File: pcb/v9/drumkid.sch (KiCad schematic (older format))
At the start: 57 parts, among them J1 DIN-5_180degree, J2 DIN-5_180degree, J3 Conn_01x15, J4 Conn_01x15, J9 AudioJack3_Ground_Switch, SW1 SW_Push, SW2 SW_Push, SW3 SW_Push, SW4 SW_Push, SW5 SW_Push, SW6 SW_Push, SW7 SW_SPDT, SW8 SW_SPDT, U1 6N138

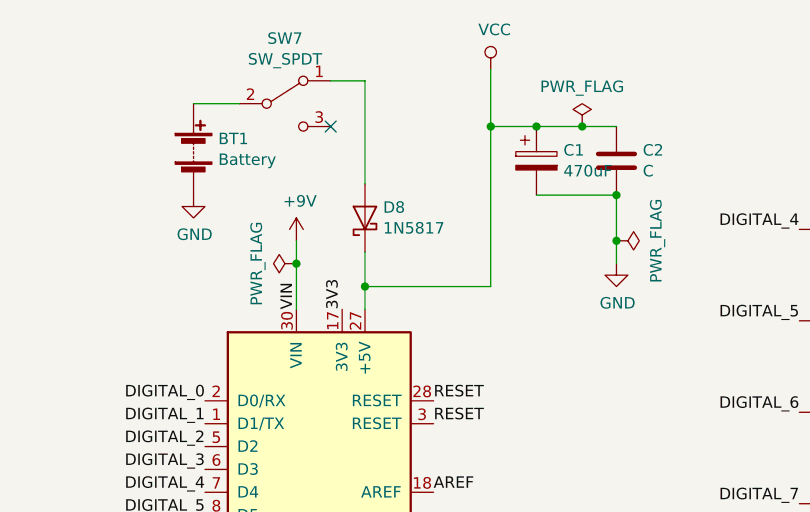
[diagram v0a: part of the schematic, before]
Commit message: added footprints for v9
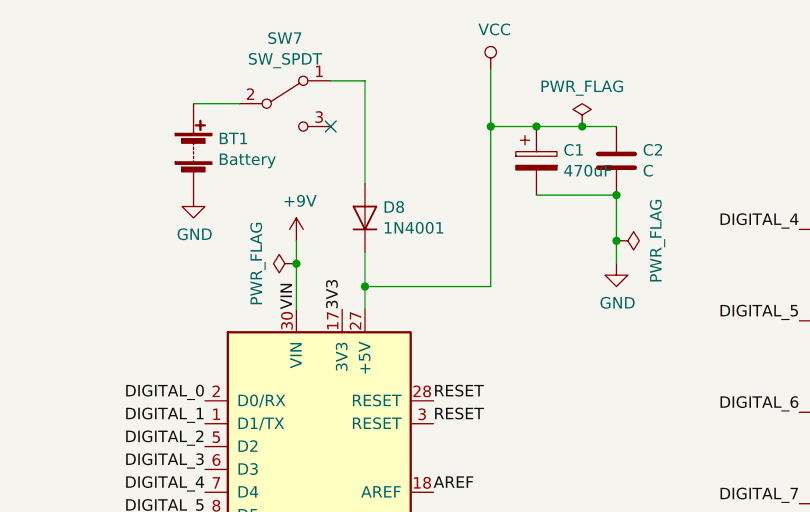
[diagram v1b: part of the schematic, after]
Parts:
- removed D8: 1N5817, symbol Diode:1N5817
- added D8: 1N4001, Diode_SMD:D_SOD-123, symbol Diode:1N4001
- BT1: footprint Connector_Wire:SolderWirePad_1x02_P5.08mm_Drill1.5mm -> Connector_Wire:SolderWire-0.5sqmm_1x02_P4.8mm_D0.9mm_OD2.3mm
- D7: footprint (none) -> Diode_SMD:D_SOD-323
- R1, R10, R11, R12, R13, R2, R3, R4, R5, R6, R7, R8, R9: footprint (none) -> Resistor_SMD:R_1206_3216Metric
- U1: footprint (none) -> Package_DIP:PowerIntegrations_SMD-8
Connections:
- net VCC: now also D8.1 (K)
- net at SW7.1 (A): now also D8.2 (A)
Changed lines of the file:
@@
 Title "DrumKid"
 Date ""
-Rev "v8"
+Rev "v9"
 Comp "by Matt Bradshaw"
 Comment1 ""
@@
 F 0 "R2" V 5243 2050 50  0000 C CNN
 F 1 "680" V 5334 2050 50  0000 C CNN
-F 2 "" V 5380 2050 50  0001 C CNN
+F 2 "Resistor_SMD:R_1206_3216Metric" V 5380 2050 50  0001 C CNN
 F 3 "~" H 5450 2050 50  0001 C CNN
 	1    5450 2050
@@
 F 0 "BT1" H 1558 1346 50  0000 L CNN
 F 1 "Battery" H 1558 1255 50  0000 L CNN
-F 2 "Connector_Wire:SolderWirePad_1x02_P5.08mm_Drill1.5mm" V 1450 1360 50  0001 C CNN
+F 2 "Connector_Wire:SolderWire-0.5sqmm_1x02_P4.8mm_D0.9mm_OD2.3mm" V 1450 1360 50  0001 C CNN
 F 3 "~" V 1450 1360 50  0001 C CNN
 	1    1450 1300
@@
 F 0 "R3" V 5243 2450 50  0000 C CNN
 F 1 "680" V 5334 2450 50  0000 C CNN
-F 2 "" V 5380 2450 50  0001 C CNN
+F 2 "Resistor_SMD:R_1206_3216Metric" V 5380 2450 50  0001 C CNN
 F 3 "~" H 5450 2450 50  0001 C CNN
 	1    5450 2450
@@
 F 0 "R4" V 5243 2850 50  0000 C CNN
 F 1 "680" V 5334 2850 50  0000 C CNN
-F 2 "" V 5380 2850 50  0001 C CNN
+F 2 "Resistor_SMD:R_1206_3216Metric" V 5380 2850 50  0001 C CNN
 F 3 "~" H 5450 2850 50  0001 C CNN
 	1    5450 2850
@@
 F 0 "R5" V 5243 3250 50  0000 C CNN
 F 1 "680" V 5334 3250 50  0000 C CNN
-F 2 "" V 5380 3250 50  0001 C CNN
+F 2 "Resistor_SMD:R_1206_3216Metric" V 5380 3250 50  0001 C CNN
 F 3 "~" H 5450 3250 50  0001 C CNN
 	1    5450 3250
@@
 F 0 "R6" V 5243 3650 50  0000 C CNN
 F 1 "680" V 5334 3650 50  0000 C CNN
-F 2 "" V 5380 3650 50  0001 C CNN
+F 2 "Resistor_SMD:R_1206_3216Metric" V 5380 3650 50  0001 C CNN
 F 3 "~" H 5450 3650 50  0001 C CNN
 	1    5450 3650
@@
 Text Label 1500 3700 2    50   ~ 0
 DIGITAL_13
-$Comp
-L Diode:1N5817 D8
-U 1 1 5E76DFE8
-P 2200 1600
-F 0 "D8" V 2246 1521 50  0000 R CNN
-F 1 "1N5817" V 2155 1521 50  0000 R CNN
-F 2 "" H 2200 1425 50  0001 C CNN
-F 3 "http://www.vishay.com/docs/88525/1n5817.pdf" H 2200 1600 50  0001 C CNN
-	1    2200 1600
-	0    -1   -1   0
-$EndComp
 Wire Wire Line
 	1450 1100 1650 1100
@@
 F 0 "R10" V 5743 5700 50  0000 C CNN
 F 1 "220" V 5834 5700 50  0000 C CNN
-F 2 "" V 5880 5700 50  0001 C CNN
+F 2 "Resistor_SMD:R_1206_3216Metric" V 5880 5700 50  0001 C CNN
 F 3 "~" H 5950 5700 50  0001 C CNN
 	1    5950 5700
@@
 F 0 "R11" V 6643 5700 50  0000 C CNN
 F 1 "220" V 6734 5700 50  0000 C CNN
-F 2 "" V 6780 5700 50  0001 C CNN
+F 2 "Resistor_SMD:R_1206_3216Metric" V 6780 5700 50  0001 C CNN
 F 3 "~" H 6850 5700 50  0001 C CNN
 	1    6850 5700
@@
 F 0 "R7" V 1143 5700 50  0000 C CNN
 F 1 "220" V 1234 5700 50  0000 C CNN
-F 2 "" V 1280 5700 50  0001 C CNN
+F 2 "Resistor_SMD:R_1206_3216Metric" V 1280 5700 50  0001 C CNN
 F 3 "~" H 1350 5700 50  0001 C CNN
 	1    1350 5700
@@
 F 0 "D7" V 1454 5929 50  0000 L CNN
 F 1 "1N4148" V 1545 5929 50  0000 L CNN
-F 2 "" H 1500 5675 50  0001 C CNN
+F 2 "Diode_SMD:D_SOD-323" H 1500 5675 50  0001 C CNN
 F 3 "http://www.nxp.com/documents/data_sheet/1N4148_1N4448.pdf" H 1500 5850 50  0001 C CNN
 	1    1500 5850
@@
 F 0 "U1" H 2350 6267 50  0000 C CNN
 F 1 "6N138" H 2350 6176 50  0000 C CNN
-F 2 "" H 2640 5500 50  0001 C CNN
+F 2 "Package_DIP:PowerIntegrations_SMD-8" H 2640 5500 50  0001 C CNN
 F 3 "http://www.onsemi.com/pub/Collateral/HCPL2731-D.pdf" H 2640 5500 50  0001 C CNN
 	1    2350 5800
@@
 F 0 "R9" V 4193 5900 50  0000 C CNN
 F 1 "470" V 4284 5900 50  0000 C CNN
-F 2 "" V 4330 5900 50  0001 C CNN
+F 2 "Resistor_SMD:R_1206_3216Metric" V 4330 5900 50  0001 C CNN
 F 3 "~" H 4400 5900 50  0001 C CNN
 	1    4400 5900
@@
 F 0 "R8" V 2593 5700 50  0000 C CNN
 F 1 "10k" V 2684 5700 50  0000 C CNN
-F 2 "" V 2730 5700 50  0001 C CNN
+F 2 "Resistor_SMD:R_1206_3216Metric" V 2730 5700 50  0001 C CNN
 F 3 "~" H 2800 5700 50  0001 C CNN
 	1    2800 5700
@@
 F 0 "R1" V 5243 1650 50  0000 C CNN
 F 1 "680" V 5334 1650 50  0000 C CNN
-F 2 "" V 5380 1650 50  0001 C CNN
+F 2 "Resistor_SMD:R_1206_3216Metric" V 5380 1650 50  0001 C CNN
 F 3 "~" H 5450 1650 50  0001 C CNN
 	1    5450 1650
@@
 F 0 "R13" V 9450 5500 50  0000 C CNN
 F 1 "1k" V 9550 5500 50  0000 C CNN
-F 2 "" V 9280 5500 50  0001 C CNN
+F 2 "Resistor_SMD:R_1206_3216Metric" V 9280 5500 50  0001 C CNN
 F 3 "~" H 9350 5500 50  0001 C CNN
 	1    9350 5500
@@
 F 0 "R12" V 9143 5300 50  0000 C CNN
 F 1 "1k" V 9234 5300 50  0000 C CNN
-F 2 "" V 9280 5300 50  0001 C CNN
+F 2 "Resistor_SMD:R_1206_3216Metric" V 9280 5300 50  0001 C CNN
 F 3 "~" H 9350 5300 50  0001 C CNN
 	1    9350 5300
@@
 	9650 5600 9650 6000
 Connection ~ 9650 6000
+$Comp
+L Diode:1N4001 D8
+U 1 1 5EF372BA
+P 2200 1600
+F 0 "D8" V 2246 1521 50  0000 R CNN
+F 1 "1N4001" V 2155 1521 50  0000 R CNN
+F 2 "Diode_SMD:D_SOD-123" H 2200 1425 50  0001 C CNN
+F 3 "http://www.vishay.com/docs/88503/1n4001.pdf" H 2200 1600 50  0001 C CNN
+	1    2200 1600
+	0    -1   -1   0
+$EndComp
 $EndSCHEMATC

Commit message: another new PCB revision, hopefully the last one for a while...
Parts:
- removed C2, C4: C, drumkidcustom:C_Disc_D3.4mm_W2.1mm_P2.50mm, symbol Device:C
- removed D8: 1N4001, Diode_SMD:D_SOD-123, symbol Diode:1N4001
- added C?: 100nF, symbol Device:C
- added D8: 1N5817, Diode_THT:D_DO-41_SOD81_P10.16mm_Horizontal, symbol Diode:1N5817
- added J? (x2): Conn_01x15, Connector_PinSocket_2.54mm:PinSocket_1x15_P2.54mm_Vertical, symbol Connector_Generic:Conn_01x15
- added J? (x4): Conn_01x10, symbol Connector_Generic:Conn_01x10
- added R?: 270, drumkidcustom:R_Axial_DIN0207_L6.3mm_D2.5mm_P10.16mm_Horizontal, symbol Device:R
- BT1: footprint Connector_Wire:SolderWire-0.5sqmm_1x02_P4.8mm_D0.9mm_OD2.3mm -> Connector_Wire:SolderWirePad_1x02_P5.08mm_Drill1.5mm
- C1, C3, C5: footprint Capacitor_SMD:CP_Elec_8x10 -> drumkidcustom:CP_Radial_D6.3mm_P2.50mm
- D7: footprint Diode_SMD:D_SOD-323 -> Diode_THT:D_DO-35_SOD27_P7.62mm_Horizontal
- R1, R2, R3, R4, R5, R6: value 680 -> R_LED; footprint Resistor_SMD:R_1206_3216Metric -> drumkidcustom:R_Axial_DIN0207_L6.3mm_D2.5mm_P10.16mm_Horizontal
- R10, R11, R12, R13, R7, R8, R9: footprint Resistor_SMD:R_1206_3216Metric -> drumkidcustom:R_Axial_DIN0207_L6.3mm_D2.5mm_P10.16mm_Horizontal
- U1: footprint Package_DIP:PowerIntegrations_SMD-8 -> Package_DIP:DIP-8_W7.62mm_Socket
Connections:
- net +9V: now also J?.15 (Pin_15)
- net 3V3: now also J?.2 (Pin_2)
- net ANALOG_0: now also J?.4 (Pin_4)
- net ANALOG_1: now also J?.5 (Pin_5)
- net ANALOG_2: now also J?.6 (Pin_6)
- net ANALOG_3: now also J?.7 (Pin_7)
- net ANALOG_4: now also J?.8 (Pin_8)
- net ANALOG_5: now also J?.9 (Pin_9)
- net ANALOG_6: now also J?.10 (Pin_10)
- net ANALOG_7: now also J?.11 (Pin_11)
- net AREF: now also J?.3 (Pin_3)
- net DIGITAL_0: now also J?.14 (Pin_14)
- net DIGITAL_1: now also J?.15 (Pin_15)
- net DIGITAL_10: now also J?.3 (Pin_3)
- net DIGITAL_11: now also J?.2 (Pin_2)
- net DIGITAL_12: now also J?.1 (Pin_1)
- net DIGITAL_13: now also J?.1 (Pin_1)
- net DIGITAL_2: now also J?.11 (Pin_11)
- net DIGITAL_3: now also J?.10 (Pin_10)
- net DIGITAL_4: now also J?.9 (Pin_9)
- net DIGITAL_5: now also J?.8 (Pin_8)
- net DIGITAL_6: now also J?.7 (Pin_7)
- net DIGITAL_7: now also J?.6 (Pin_6)
- net DIGITAL_8: now also J?.5 (Pin_5)
- net DIGITAL_9: now also J?.4 (Pin_4), R?.2; no longer RV5.1
- net GND: now also C?.2, J?.12 (Pin_12), J?.14 (Pin_14)
- net RESET: now also J?.13 (Pin_13), J?.13 (Pin_13)
- net VCC: now also D8.1 (K), J?.12 (Pin_12)
- net at SW7.1 (A): now also D8.2 (A)
- new net: C?.1, R?.1, RV5.1
- new net: J?.1 (Pin_1), J?.1 (Pin_1) (x2)
- new net: J?.10 (Pin_10), J?.10 (Pin_10) (x2)
- new net: J?.2 (Pin_2), J?.2 (Pin_2) (x2)
- new net: J?.3 (Pin_3), J?.3 (Pin_3) (x2)
- new net: J?.4 (Pin_4), J?.4 (Pin_4) (x2)
- new net: J?.5 (Pin_5), J?.5 (Pin_5) (x2)
- new net: J?.6 (Pin_6), J?.6 (Pin_6) (x2)
- new net: J?.7 (Pin_7), J?.7 (Pin_7) (x2)
- new net: J?.8 (Pin_8), J?.8 (Pin_8) (x2)
- new net: J?.9 (Pin_9), J?.9 (Pin_9) (x2)
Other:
- note added: "Extra holes to enable adding\nstripboard modifications"
- moved on the sheet: C5, H1, H10, H2, H3, H4, H5, H6, H7, H8, H9, J9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

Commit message: making space for new bits
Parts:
- C2: renamed from C?; footprint (none) -> Capacitor_THT:C_Disc_D3.0mm_W1.6mm_P2.50mm
- J5, J6, J7, J8: renamed from J?; footprint (none) -> Connector_PinSocket_2.54mm:PinSocket_1x10_P2.54mm_Vertical
- gave numbers to parts that had none: 3
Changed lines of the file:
@@
 Title "DrumKid"
 Date ""
-Rev "v8"
+Rev "v9"
 Comp "by Matt Bradshaw"
 Comment1 ""
@@
 Connection ~ 10050 6000
 $Comp
-L Device:R R?
+L Device:R R14
 U 1 1 5F2845DE
 P 8050 5600
-F 0 "R?" V 7843 5600 50  0000 C CNN
+F 0 "R14" V 7843 5600 50  0000 C CNN
 F 1 "270" V 7934 5600 50  0000 C CNN
 F 2 "drumkidcustom:R_Axial_DIN0207_L6.3mm_D2.5mm_P10.16mm_Horizontal" V 7980 5600 50  0001 C CNN
@@
 	8900 5600 9200 5600
 $Comp
-L Device:C C?
+L Device:C C2
 U 1 1 5F2A0A75
 P 8300 5850
-F 0 "C?" H 8415 5896 50  0000 L CNN
+F 0 "C2" H 8415 5896 50  0000 L CNN
 F 1 "100nF" H 8415 5805 50  0000 L CNN
-F 2 "" H 8338 5700 50  0001 C CNN
+F 2 "Capacitor_THT:C_Disc_D3.0mm_W1.6mm_P2.50mm" H 8338 5700 50  0001 C CNN
 F 3 "~" H 8300 5850 50  0001 C CNN
 	1    8300 5850
@@
 	7450 5600 7900 5600
 $Comp
-L Connector_Generic:Conn_01x15 J?
+L Connector_Generic:Conn_01x15 J10
 U 1 1 5F2D1783
 P 10150 2300
-F 0 "J?" H 10230 2342 50  0000 L CNN
+F 0 "J10" H 10230 2342 50  0000 L CNN
 F 1 "Conn_01x15" H 10230 2251 50  0000 L CNN
 F 2 "Connector_PinSocket_2.54mm:PinSocket_1x15_P2.54mm_Vertical" H 10150 2300 50  0001 C CNN
@@
 ANALOG_7
 $Comp
-L Connector_Generic:Conn_01x15 J?
+L Connector_Generic:Conn_01x15 J11
 U 1 1 5F2D1791
 P 10150 3950
-F 0 "J?" H 10230 3992 50  0000 L CNN
+F 0 "J11" H 10230 3992 50  0000 L CNN
 F 1 "Conn_01x15" H 10230 3901 50  0000 L CNN
 F 2 "Connector_PinSocket_2.54mm:PinSocket_1x15_P2.54mm_Vertical" H 10150 3950 50  0001 C CNN
@@
 3V3
 $Comp
-L power:VCC #PWR?
+L power:VCC #PWR01
 U 1 1 5F2D17AA
 P 9400 1500
-F 0 "#PWR?" H 9400 1350 50  0001 C CNN
+F 0 "#PWR01" H 9400 1350 50  0001 C CNN
 F 1 "VCC" H 9417 1673 50  0000 C CNN
 F 2 "" H 9400 1500 50  0001 C CNN
@@
 $EndComp
 $Comp
-L power:GND #PWR?
+L power:GND #PWR02
 U 1 1 5F2D17B0
 P 9400 4650
-F 0 "#PWR?" H 9400 4400 50  0001 C CNN
+F 0 "#PWR02" H 9400 4400 50  0001 C CNN
 F 1 "GND" H 9405 4477 50  0000 C CNN
 F 2 "" H 9400 4650 50  0001 C CNN
@@
 $EndComp
 $Comp
-L Connector_Generic:Conn_01x10 J?
+L Connector_Generic:Conn_01x10 J5
 U 1 1 5F2F774B
 P 3950 7100
-F 0 "J?" H 3800 7800 50  0000 L CNN
+F 0 "J5" H 3800 7800 50  0000 L CNN
 F 1 "Conn_01x10" H 3600 7700 50  0000 L CNN
-F 2 "" H 3950 7100 50  0001 C CNN
+F 2 "Connector_PinSocket_2.54mm:PinSocket_1x10_P2.54mm_Vertical" H 3950 7100 50  0001 C CNN
 F 3 "~" H 3950 7100 50  0001 C CNN
 	1    3950 7100
@@
 $EndComp
 $Comp
-L Connector_Generic:Conn_01x10 J?
+L Connector_Generic:Conn_01x10 J6
 U 1 1 5F2F97BE
 P 4300 7100
-F 0 "J?" H 4250 7800 50  0000 L CNN
+F 0 "J6" H 4250 7800 50  0000 L CNN
 F 1 "Conn_01x10" H 4100 7700 50  0000 L CNN
-F 2 "" H 4300 7100 50  0001 C CNN
+F 2 "Connector_PinSocket_2.54mm:PinSocket_1x10_P2.54mm_Vertical" H 4300 7100 50  0001 C CNN
 F 3 "~" H 4300 7100 50  0001 C CNN
 	1    4300 7100
@@
 	3750 7600 4100 7600
 $Comp
-L Connector_Generic:Conn_01x10 J?
+L Connector_Generic:Conn_01x10 J7
 U 1 1 5F336643
 P 4950 7100
-F 0 "J?" H 4800 7800 50  0000 L CNN
+F 0 "J7" H 4800 7800 50  0000 L CNN
 F 1 "Conn_01x10" H 4600 7700 50  0000 L CNN
-F 2 "" H 4950 7100 50  0001 C CNN
+F 2 "Connector_PinSocket_2.54mm:PinSocket_1x10_P2.54mm_Vertical" H 4950 7100 50  0001 C CNN
 F 3 "~" H 4950 7100 50  0001 C CNN
 	1    4950 7100
@@
 $EndComp
 $Comp
-L Connector_Generic:Conn_01x10 J?
+L Connector_Generic:Conn_01x10 J8
 U 1 1 5F336649
 P 5300 7100
-F 0 "J?" H 5250 7800 50  0000 L CNN
+F 0 "J8" H 5250 7800 50  0000 L CNN
 F 1 "Conn_01x10" H 5100 7700 50  0000 L CNN
-F 2 "" H 5300 7100 50  0001 C CNN
+F 2 "Connector_PinSocket_2.54mm:PinSocket_1x10_P2.54mm_Vertical" H 5300 7100 50  0001 C CNN
 F 3 "~" H 5300 7100 50  0001 C CNN
 	1    5300 7100

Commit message: may have squeezed too many things onto the PCB...
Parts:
- added J12, J14: Conn_01x05, Connector_PinSocket_2.54mm:PinSocket_1x05_P2.54mm_Vertical, symbol Connector_Generic:Conn_01x05
- added J13, J15: AudioJack3_Ground_Switch, drumkidcustom:Tayda_3.5mm_stereo_TRS_jack_A-853, symbol drumkid-rescue:AudioJack3_Ground_Switch-Connector
- J10, J11: footprint Connector_PinSocket_2.54mm:PinSocket_1x15_P2.54mm_Vertical -> Connector_PinHeader_2.54mm:PinHeader_1x15_P2.54mm_Vertical
- J6, J7: footprint Connector_PinSocket_2.54mm:PinSocket_1x10_P2.54mm_Vertical -> Connector_PinHeader_2.54mm:PinHeader_1x10_P2.54mm_Vertical
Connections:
- new net: J14.1 (Pin_1), J15.R
- new net: J14.2 (Pin_2), J15.RN
- new net: J14.3 (Pin_3), J15.S
- new net: J14.5 (Pin_5), J15.T
- new net: J14.4 (Pin_4), J15.TN
- new net: J12.1 (Pin_1), J13.R
- new net: J12.2 (Pin_2), J13.RN
- new net: J12.3 (Pin_3), J13.S
- new net: J12.5 (Pin_5), J13.T
- new net: J12.4 (Pin_4), J13.TN
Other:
- note added: "Extra 3.5mm socket footprints\nin case of hacking (Eurorack?)"
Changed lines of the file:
@@
 F 0 "J10" H 10230 2342 50  0000 L CNN
 F 1 "Conn_01x15" H 10230 2251 50  0000 L CNN
-F 2 "Connector_PinSocket_2.54mm:PinSocket_1x15_P2.54mm_Vertical" H 10150 2300 50  0001 C CNN
+F 2 "Connector_PinHeader_2.54mm:PinHeader_1x15_P2.54mm_Vertical" H 10150 2300 50  0001 C CNN
 F 3 "~" H 10150 2300 50  0001 C CNN
 	1    10150 2300
@@
 F 0 "J11" H 10230 3992 50  0000 L CNN
 F 1 "Conn_01x15" H 10230 3901 50  0000 L CNN
-F 2 "Connector_PinSocket_2.54mm:PinSocket_1x15_P2.54mm_Vertical" H 10150 3950 50  0001 C CNN
+F 2 "Connector_PinHeader_2.54mm:PinHeader_1x15_P2.54mm_Vertical" H 10150 3950 50  0001 C CNN
 F 3 "~" H 10150 3950 50  0001 C CNN
 	1    10150 3950
@@
 F 0 "J6" H 4250 7800 50  0000 L CNN
 F 1 "Conn_01x10" H 4100 7700 50  0000 L CNN
-F 2 "Connector_PinSocket_2.54mm:PinSocket_1x10_P2.54mm_Vertical" H 4300 7100 50  0001 C CNN
+F 2 "Connector_PinHeader_2.54mm:PinHeader_1x10_P2.54mm_Vertical" H 4300 7100 50  0001 C CNN
 F 3 "~" H 4300 7100 50  0001 C CNN
 	1    4300 7100
@@
 F 0 "J7" H 4800 7800 50  0000 L CNN
 F 1 "Conn_01x10" H 4600 7700 50  0000 L CNN
-F 2 "Connector_PinSocket_2.54mm:PinSocket_1x10_P2.54mm_Vertical" H 4950 7100 50  0001 C CNN
+F 2 "Connector_PinHeader_2.54mm:PinHeader_1x10_P2.54mm_Vertical" H 4950 7100 50  0001 C CNN
 F 3 "~" H 4950 7100 50  0001 C CNN
 	1    4950 7100
@@
 Text Notes 5550 6900 0    50   ~ 0
 Extra holes to enable adding\nstripboard modifications
+$Comp
+L drumkid-rescue:AudioJack3_Ground_Switch-Connector J15
+U 1 1 5F38384E
+P 7200 900
+F 0 "J15" H 6850 800 50  0000 R CNN
+F 1 "AudioJack3_Ground_Switch" H 6950 700 50  0000 R CNN
+F 2 "drumkidcustom:Tayda_3.5mm_stereo_TRS_jack_A-853" H 7200 900 50  0001 C CNN
+F 3 "~" H 7200 900 50  0001 C CNN
+	1    7200 900
+	-1   0    0    1
+$EndComp
+$Comp
+L Connector_Generic:Conn_01x05 J14
+U 1 1 5F383854
+P 6500 800
+F 0 "J14" H 6800 800 50  0000 C CNN
+F 1 "Conn_01x05" H 6800 700 50  0000 C CNN
+F 2 "Connector_PinSocket_2.54mm:PinSocket_1x05_P2.54mm_Vertical" H 6500 800 50  0001 C CNN
+F 3 "~" H 6500 800 50  0001 C CNN
+	1    6500 800
+	-1   0    0    1
+$EndComp
+Text Notes 5050 1050 0    50   ~ 0
+Extra 3.5mm socket footprints\nin case of hacking (Eurorack?)
+Wire Wire Line
+	6700 1000 6900 1000
+Wire Wire Line
+	6900 1000 6900 900
+Wire Wire Line
+	6900 900  7000 900
+Wire Wire Line
+	7000 1000 6950 1000
+Wire Wire Line
+	6950 1000 6950 950
+Wire Wire Line
+	6950 950  6850 950
+Wire Wire Line
+	6850 950  6850 800
+Wire Wire Line
+	6850 800  6700 800
+Wire Wire Line
+	6800 900  6800 850
+Wire Wire Line
+	6800 850  7000 850
+Wire Wire Line
+	7000 850  7000 800
+Wire Wire Line
+	6700 900  6800 900
+Wire Wire Line
+	6700 700  6900 700
+Wire Wire Line
+	6900 700  6900 600
+Wire Wire Line
+	6900 600  7000 600
+Wire Wire Line
+	7000 700  6950 700
+Wire Wire Line
+	6950 700  6950 650
+Wire Wire Line
+	6950 650  6700 650
+Wire Wire Line
+	6700 650  6700 600
+$Comp
+L drumkid-rescue:AudioJack3_Ground_Switch-Connector J13
+U 1 1 5F3BF4C6
+P 4650 900
+F 0 "J13" H 4300 800 50  0000 R CNN
+F 1 "AudioJack3_Ground_Switch" H 4400 700 50  0000 R CNN
+F 2 "drumkidcustom:Tayda_3.5mm_stereo_TRS_jack_A-853" H 4650 900 50  0001 C CNN
+F 3 "~" H 4650 900 50  0001 C CNN
+	1    4650 900
+	-1   0    0    1
+$EndComp
+$Comp
+L Connector_Generic:Conn_01x05 J12
+U 1 1 5F3BF4CC
+P 3950 800
+F 0 "J12" H 4250 800 50  0000 C CNN
+F 1 "Conn_01x05" H 4250 700 50  0000 C CNN
+F 2 "Connector_PinSocket_2.54mm:PinSocket_1x05_P2.54mm_Vertical" H 3950 800 50  0001 C CNN
+F 3 "~" H 3950 800 50  0001 C CNN
+	1    3950 800
+	-1   0    0    1
+$EndComp
+Wire Wire Line
+	4350 1000 4350 900
+Wire Wire Line
+	4350 900  4450 900
+Wire Wire Line
+	4400 1000 4400 950
+Wire Wire Line
+	4400 950  4300 950
+Wire Wire Line
+	4300 950  4300 800
+Wire Wire Line
+	4300 800  4150 800
+Wire Wire Line
+	4250 900  4250 850
+Wire Wire Line
+	4250 850  4450 850
+Wire Wire Line
+	4450 850  4450 800
+Wire Wire Line
+	4150 900  4250 900
+Wire Wire Line
+	4150 700  4350 700
+Wire Wire Line
+	4350 700  4350 600
+Wire Wire Line
+	4350 600  4450 600
+Wire Wire Line
+	4450 700  4400 700
+Wire Wire Line
+	4400 700  4400 650
+Wire Wire Line
+	4400 650  4150 650
+Wire Wire Line
+	4150 650  4150 600
+Wire Wire Line
+	4400 1000 4450 1000
+Wire Wire Line
+	4350 1000 4150 1000
 $EndSCHEMATC
